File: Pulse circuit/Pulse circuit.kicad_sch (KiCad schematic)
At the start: 4 parts, among them U1 module_max30102, U2 module_max30102, U3 DOIT-ESP32-DEVKIT-V1

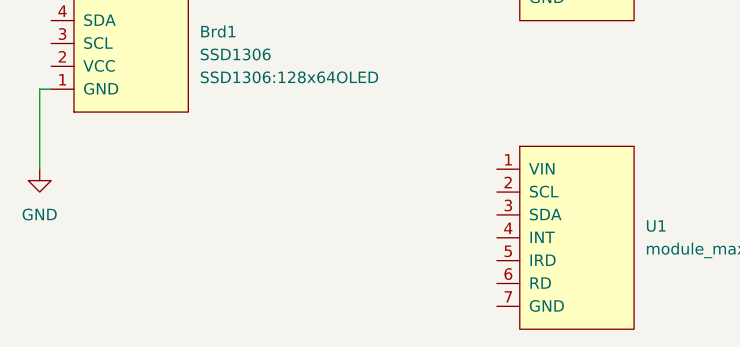
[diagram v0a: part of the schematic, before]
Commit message: Power & GND added
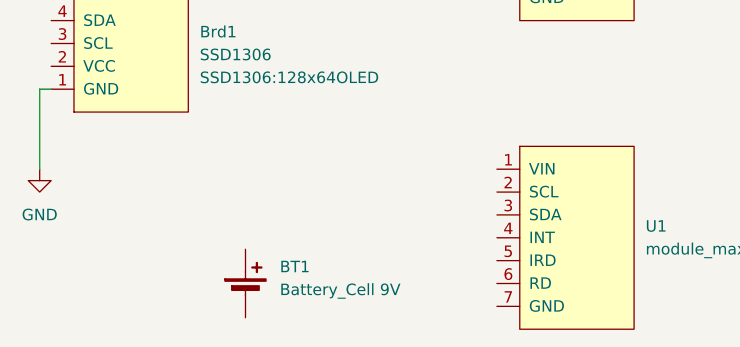
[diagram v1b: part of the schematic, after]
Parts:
- added BT1: Battery_Cell 9V, symbol Device:Battery_Cell
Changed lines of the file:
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@@
+	)
+	(symbol
+		(lib_id "Device:Battery_Cell")
+		(at 104.14 96.52 0)
+		(unit 1)
+		(exclude_from_sim no)
+		(in_bom yes)
+		(on_board yes)
+		(dnp no)
+		(fields_autoplaced yes)
+		(property "Reference" "BT1"
+			(at 107.95 93.4084 0)
+			(effects
+				(font
+					(size 1.27 1.27)
+				)
+				(justify left)
+			)
+		)
+		(property "Value" "Battery_Cell 9V"
+			(at 107.95 95.9484 0)
+			(effects
+				(font
+					(size 1.27 1.27)
+				)
+				(justify left)
+			)
+		)
+		(property "Footprint" ""
+			(at 104.14 94.996 90)
+			(effects
+				(font
+					(size 1.27 1.27)
+				)
+				(hide yes)
+			)
+		)
+		(property "Datasheet" "~"
+			(at 104.14 94.996 90)
+			(effects
+				(font
+					(size 1.27 1.27)
+				)
+				(hide yes)
+			)
+		)
+		(property "Description" "Single-cell battery"
+			(at 104.14 96.52 0)
+			(effects
+				(font
+					(size 1.27 1.27)
+				)
+				(hide yes)
+			)
+		)
+		(pin "2"
+		)
+		(pin "1"
+		)
+		(instances
+			(project ""
+				(path "/59caed24-c499-43df-90b9-3ac3a8609322"
+					(reference "BT1")
+					(unit 1)
+				)
+			)
+		)
 	)
 	(symbol

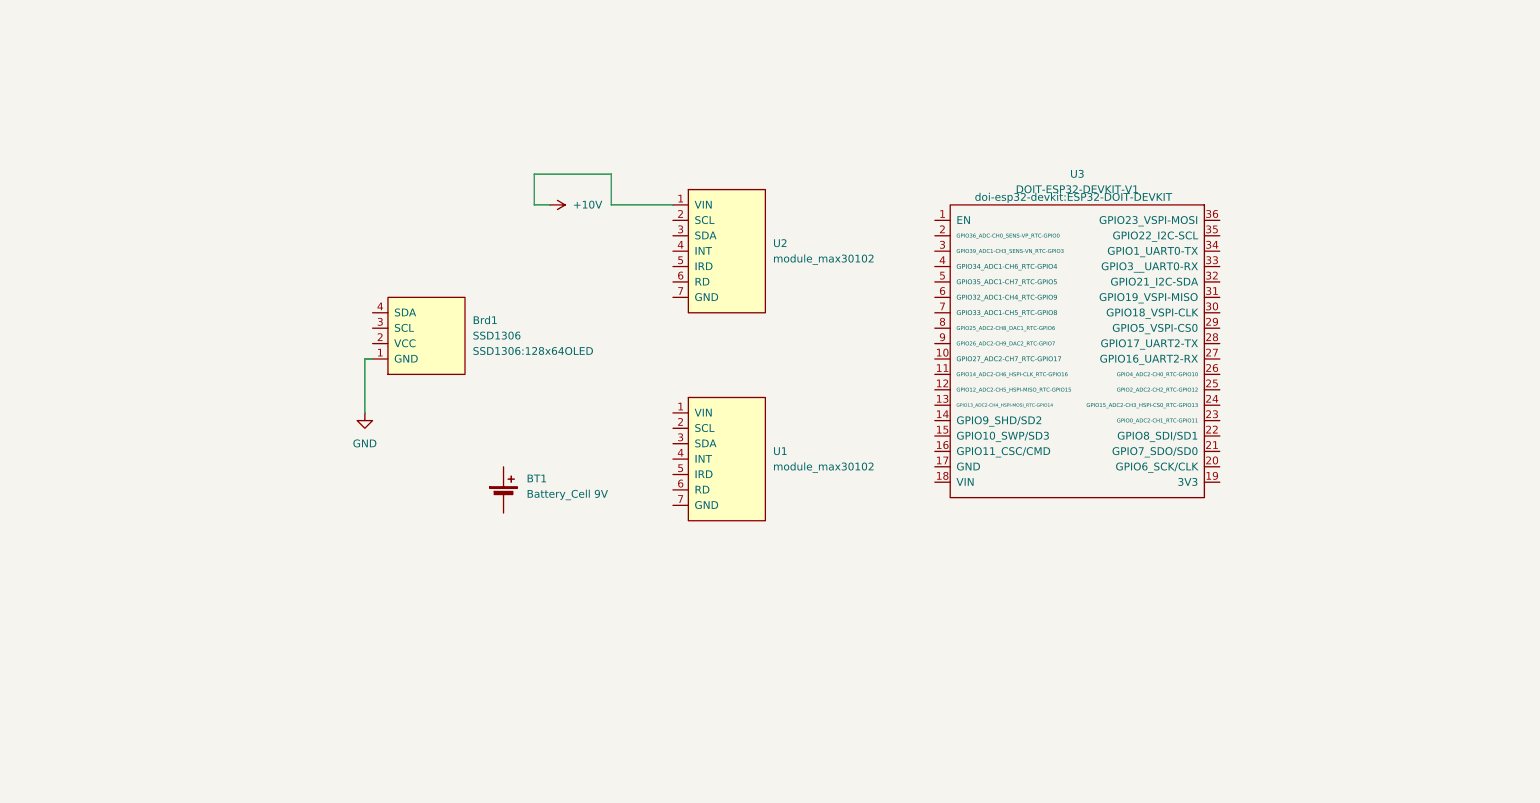
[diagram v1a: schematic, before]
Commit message: Power & GND added
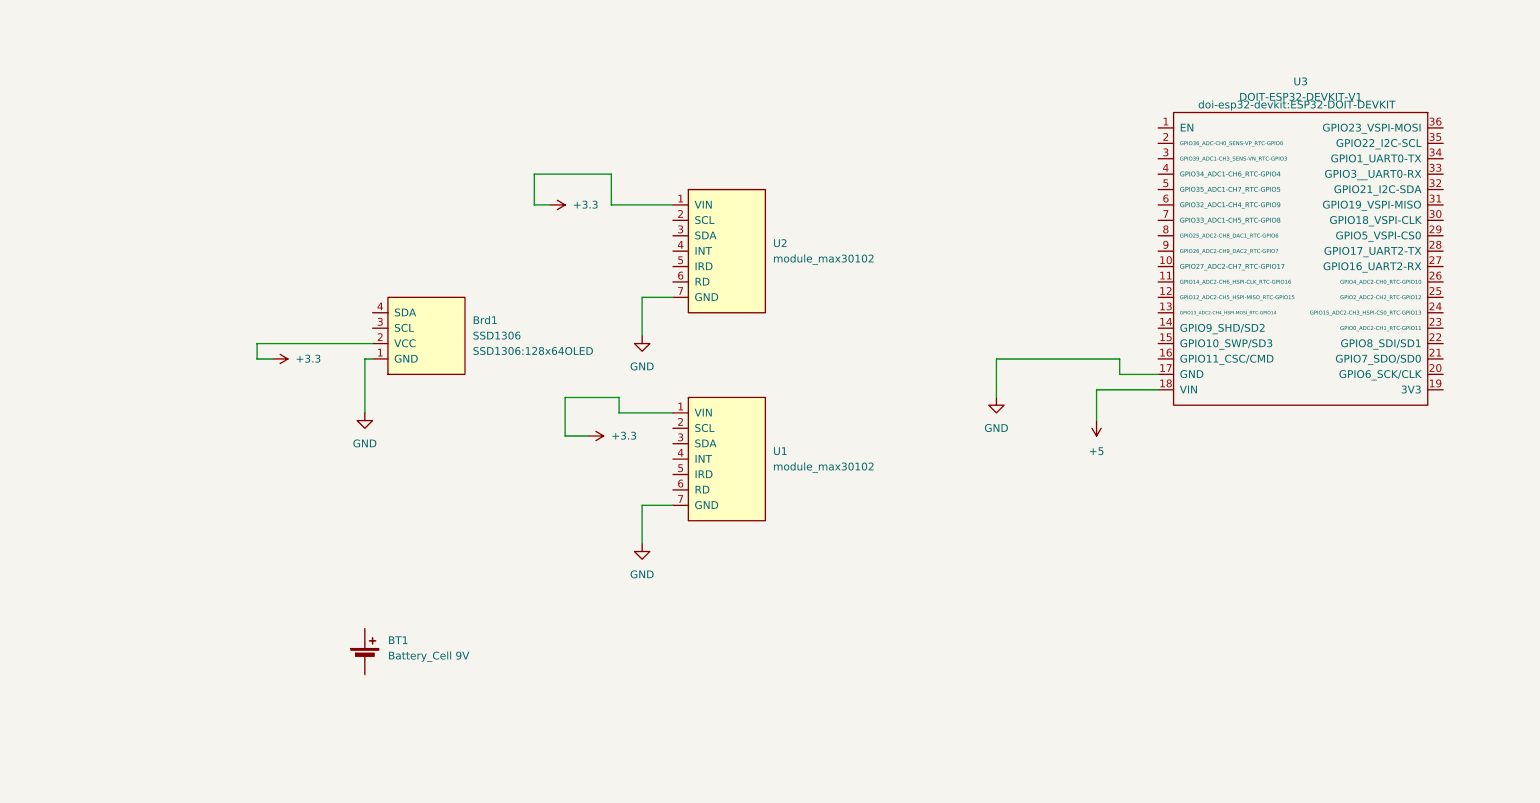
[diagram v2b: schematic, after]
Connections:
- net +10V is gone; now on net +3.3: U2.1 (VIN)
- net GND: now also U1.7 (GND), U2.7 (GND), U3.17 (GND)
- net +3.3: now reaches U1.1 (VIN)
- net +3.3: now also Brd1.2 (VCC)
- net +5: now reaches U3.18 (VIN)
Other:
- moved on the sheet: BT1, U3

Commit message: Not finished yet [Will do a revision tomorrow]
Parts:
- added U4: TCA9548APWR, Package_SO:TSSOP-24_4.4x7.8mm_P0.65mm, symbol Interface_Expansion:TCA9548APWR
- added U5: AMS1117-3.3, Package_TO_SOT_SMD:SOT-223-3_TabPin2, symbol Regulator_Linear:AMS1117-3.3
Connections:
- net GND: now also BT1.2 (-), U5.1 (GND)
- net at BT1.1 (+): now also U5.3 (VI)
- net at U1.2 (SCL): now also U4.7 (SC1)
- net at U1.3 (SDA): now also U4.6 (SD1)
- net at U2.2 (SCL): now also U4.5 (SC0)
- net at U2.3 (SDA): now also U4.4 (SD0)
- net at U3.32 (GPIO21_I2C-SDA): now also Brd1.4 (SDA), U4.23 (SDA)
- net at U3.35 (GPIO22_I2C-SCL): now also Brd1.3 (SCL), U4.22 (SCL)
- net +3.3: no longer names the net of Brd1.2 (VCC), U1.1 (VIN), U2.1 (VIN)
- net +3.3: now also U4.24 (VCC), U5.2 (VO)
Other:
- moved on the sheet: BT1, Brd1, U1, U2, U3

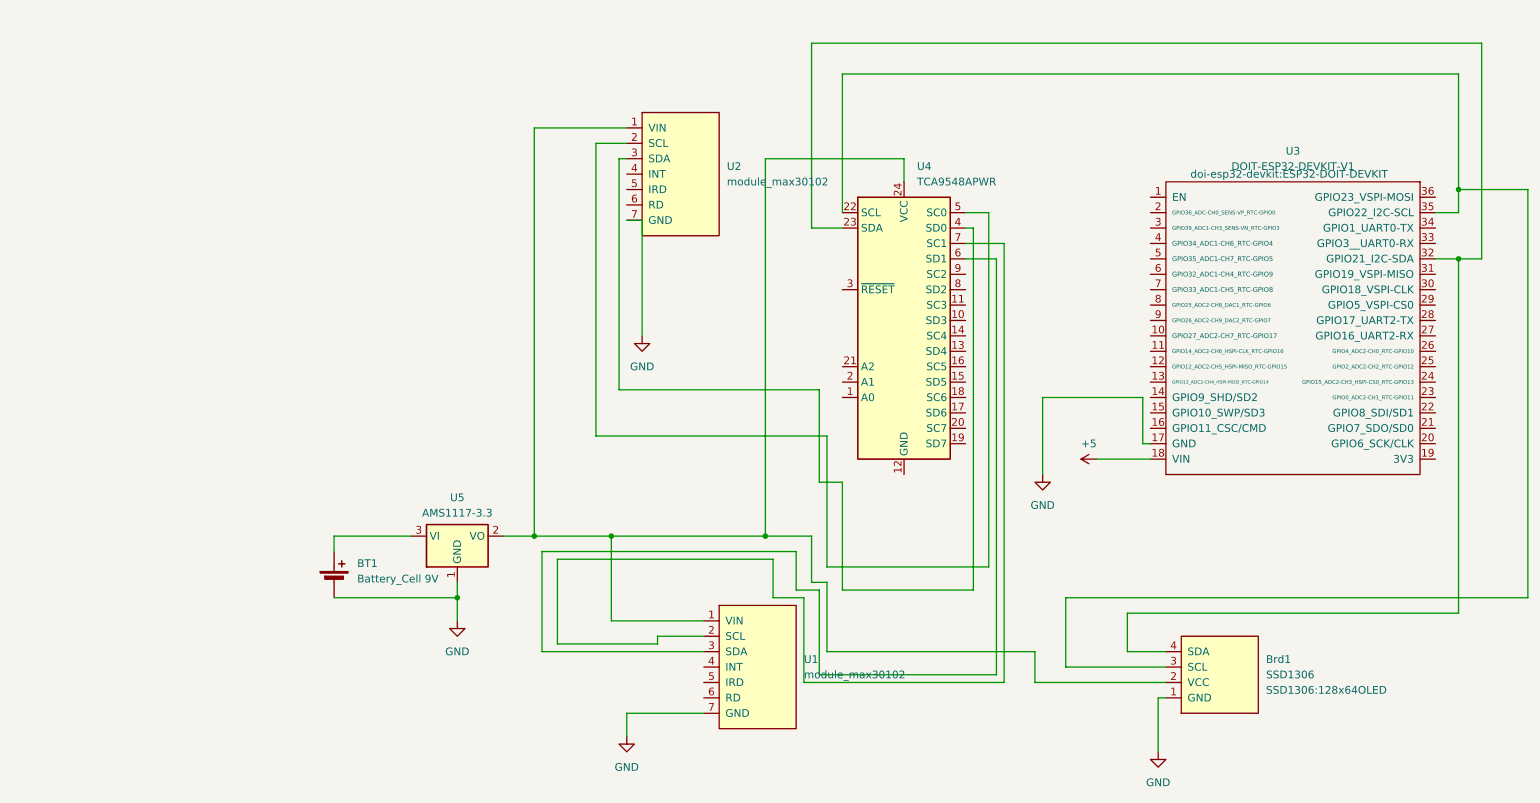
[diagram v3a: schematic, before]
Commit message: Compacted schematic - No PCB yet
-Based on Arli's schematic compacted all the wiring. Will attach picture of her wiring to help with the PCB design.
-Prepared Asila's buck converter schematic, a sheet that can be used to improve the product later with an on board voltage regulator.
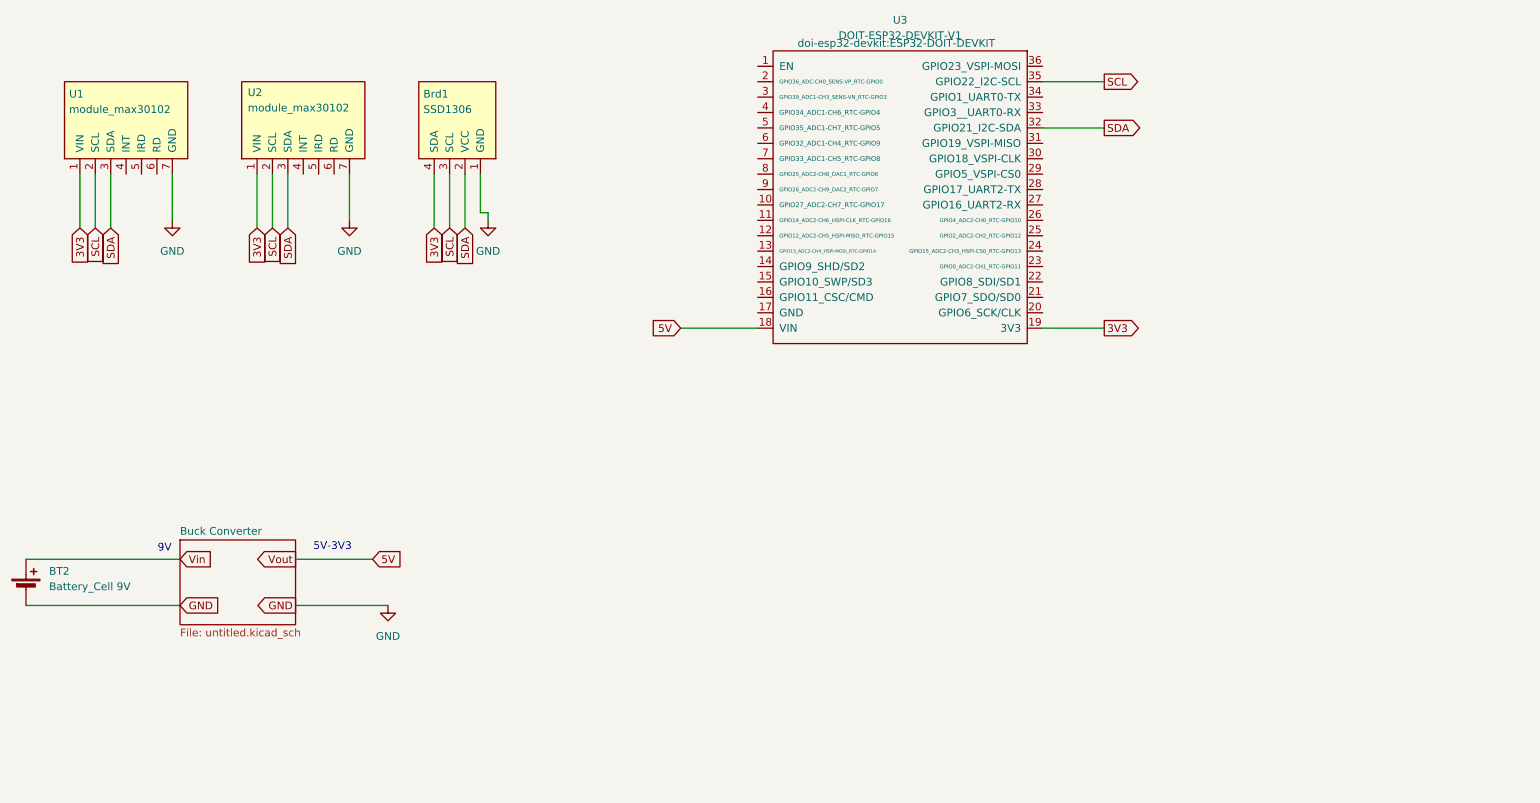
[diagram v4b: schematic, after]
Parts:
- removed BT1: Battery_Cell 9V, symbol Device:Battery_Cell
- removed U4: TCA9548APWR, Package_SO:TSSOP-24_4.4x7.8mm_P0.65mm, symbol Interface_Expansion:TCA9548APWR
- removed U5: AMS1117-3.3, Package_TO_SOT_SMD:SOT-223-3_TabPin2, symbol Regulator_Linear:AMS1117-3.3
- added BT2: Battery_Cell 9V, symbol Device:Battery_Cell
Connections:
- net GND: now also BT2.2 (-); no longer U3.17 (GND)
- net 3V3: now reaches U1.1 (VIN), U2.1 (VIN)
- net 3V3: now also Brd1.4 (SDA), U3.19 (3V3); no longer Brd1.2 (VCC)
- net SCL: now reaches U1.2 (SCL)
- net SCL: now also Brd1.3 (SCL), U2.2 (SCL), U3.35 (GPIO22_I2C-SCL)
- net SDA: now reaches U1.3 (SDA)
- net SDA: now also Brd1.2 (VCC), U2.3 (SDA), U3.32 (GPIO21_I2C-SDA)
- net +5 renamed 5V
- new net Vin: BT2.1 (+)
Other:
- added sheet Buck Converter (untitled.kicad_sch)
- note added: "5V-3V3"
- note added: "9V"
- moved on the sheet: Brd1, U1, U2, U3

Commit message: new buck converter file created
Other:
- added sheet New Buck Converter (new_buck_converter.kicad_sch)
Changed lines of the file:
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@@
+		)
+	)
+	(global_label "GND"
+		(shape input)
+		(at 127 104.14 180)
+		(fields_autoplaced yes)
+		(effects
+			(font
+				(size 1.27 1.27)
+			)
+			(justify right)
+		)
+		(property "Intersheetrefs" "${INTERSHEET_REFS}"
+			(at 120.1443 104.14 0)
+			(effects
+				(font
+					(size 1.27 1.27)
+				)
+				(justify right)
+				(hide yes)
+			)
 		)
 	)
@@
 				)
 				(justify right)
+				(hide yes)
+			)
+		)
+	)
+	(global_label "GND"
+		(shape input)
+		(at 109.22 104.14 0)
+		(fields_autoplaced yes)
+		(effects
+			(font
+				(size 1.27 1.27)
+			)
+			(justify left)
+		)
+		(property "Intersheetrefs" "${INTERSHEET_REFS}"
+			(at 116.0757 104.14 0)
+			(effects
+				(font
+					(size 1.27 1.27)
+				)
+				(justify left)
 				(hide yes)
 			)
@@
 		)
 	)
+	(global_label "Vout"
+		(shape input)
+		(at 127 97.79 180)
+		(fields_autoplaced yes)
+		(effects
+			(font
+				(size 1.27 1.27)
+			)
+			(justify right)
+		)
+		(property "Intersheetrefs" "${INTERSHEET_REFS}"
+			(at 119.9025 97.79 0)
+			(effects
+				(font
+					(size 1.27 1.27)
+				)
+				(justify right)
+				(hide yes)
+			)
+		)
+	)
 	(global_label "GND"
 		(shape input)
@@
 		(property "Intersheetrefs" "${INTERSHEET_REFS}"
 			(at 57.6557 114.3 0)
+			(effects
+				(font
+					(size 1.27 1.27)
+				)
+				(justify left)
+				(hide yes)
+			)
+		)
+	)
+	(global_label "Vin"
+		(shape input)
+		(at 109.22 97.79 0)
+		(fields_autoplaced yes)
+		(effects
+			(font
+				(size 1.27 1.27)
+			)
+			(justify left)
+		)
+		(property "Intersheetrefs" "${INTERSHEET_REFS}"
+			(at 115.0476 97.79 0)
 			(effects
 				(font
@@
 				)
 			)
+		)
+	)
+	(sheet
+		(at 109.22 93.98)
+		(size 17.78 13.97)
+		(exclude_from_sim no)
+		(in_bom yes)
+		(on_board yes)
+		(dnp no)
+		(fields_autoplaced yes)
+		(stroke
+			(width 0.1524)
+			(type solid)
+		)
+		(fill
+			(color 0 0 0 0.0000)
+		)
+		(property "Sheetname" "New Buck Converter"
+			(at 109.22 93.2684 0)
+			(effects
+				(font
+					(size 1.27 1.27)
+				)
+				(justify left bottom)
+			)
+		)
+		(property "Sheetfile" "new_buck_converter.kicad_sch"
+			(at 109.22 108.5346 0)
+			(effects
+				(font
+					(size 1.27 1.27)
+				)
+				(justify left top)
+			)
+		)
+		(instances
+			(project "Pulse circuit"
+				(path "/59caed24-c499-43df-90b9-3ac3a8609322"
+					(page "3")
+				)
+			)

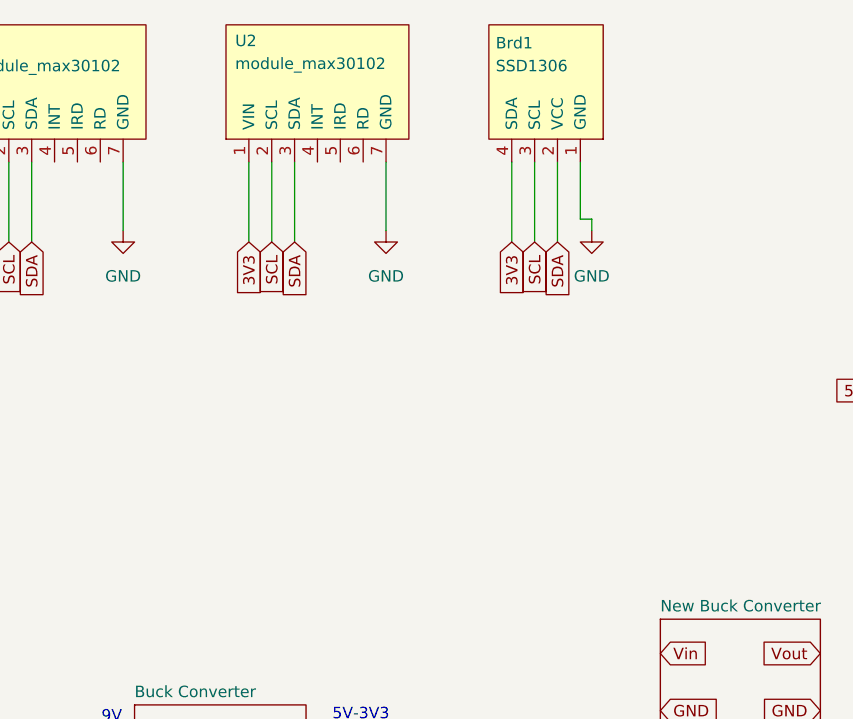
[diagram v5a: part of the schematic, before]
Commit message: Added 2 pull up resistors
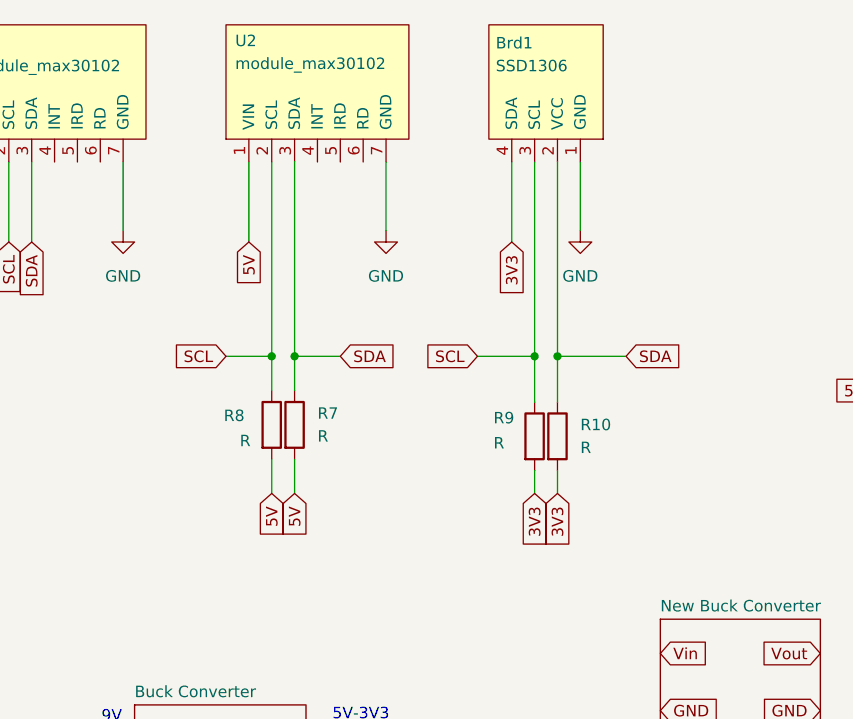
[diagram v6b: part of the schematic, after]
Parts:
- added R10, R7, R8, R9: R, symbol Device:R
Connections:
- net 3V3: now also R10.2, R9.2; no longer U2.1 (VIN)
- net 5V: now also U2.1 (VIN), R7.2, R8.2
- net SCL: now also R8.1, R9.1
- net SDA: now also R10.1, R7.1

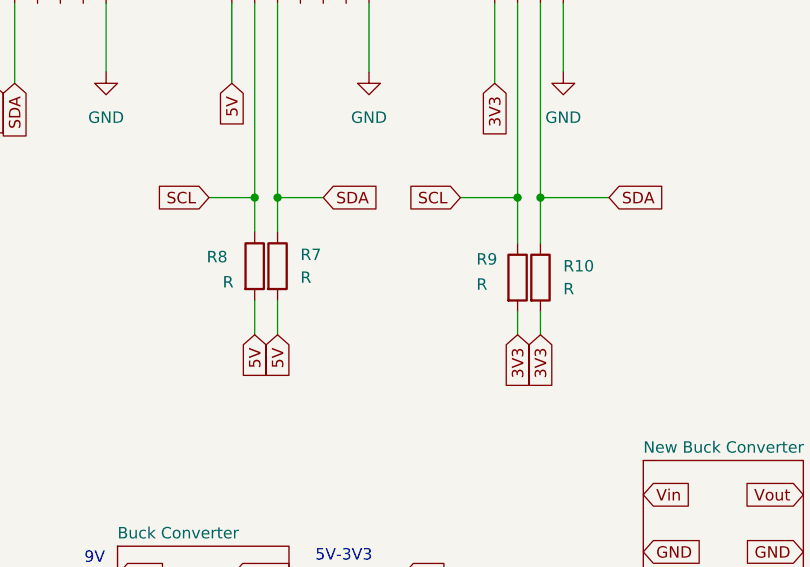
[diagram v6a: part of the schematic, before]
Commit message: Changed the R values
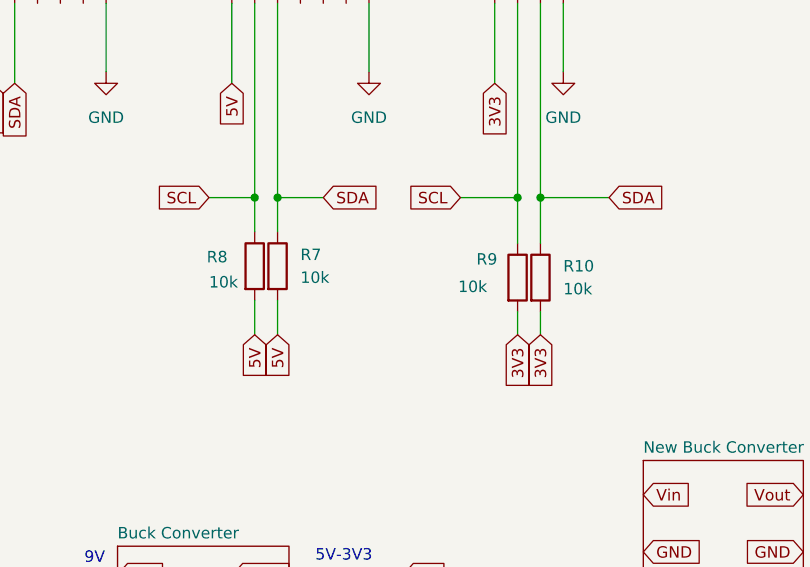
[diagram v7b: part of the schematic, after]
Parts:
- R10, R7, R8, R9: value R -> 10k
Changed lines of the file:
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@@
 			)
 		)
-		(property "Value" "R"
-			(at 62.484 74.168 0)
+		(property "Value" "10k"
+			(at 60.96 74.168 0)
 			(effects
 				(font
@@
 			)
 		)
-		(property "Value" "R"
+		(property "Value" "10k"
 			(at 100.33 74.9299 0)
 			(effects
@@
 			)
 		)
-		(property "Value" "R"
-			(at 90.678 74.422 0)
+		(property "Value" "10k"
+			(at 88.646 74.676 0)
 			(effects
 				(font
@@
 			)
 		)
-		(property "Value" "R"
+		(property "Value" "10k"
 			(at 71.12 73.6599 0)
 			(effects
